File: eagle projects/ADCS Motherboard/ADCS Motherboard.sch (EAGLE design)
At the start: 143 parts, among them J1 HDR_10_EZFET_DEBUGGER, J11 CNC_3221-10-0300-00, J3 CNC_3221-10-0300-00, J5 CNC_3221-10-0300-00, J7 TE-1734829-3, J8 CNC_3221-10-0300-00, J9 CNC_3221-14-0300-00, Q1 PMV16XN, Q2 IRLML6246TRPBF, Q3 IRLML2246TRPBF, U1 MSP430F5529IPN, U2 LMV321, U3 ADS7841E_2K5, U4 LMV321, U5 LMV321, U7 HMC1053, Y1 32.768kHz, Y2 CSTCR4M00G15L99, Y3 32.768kHz

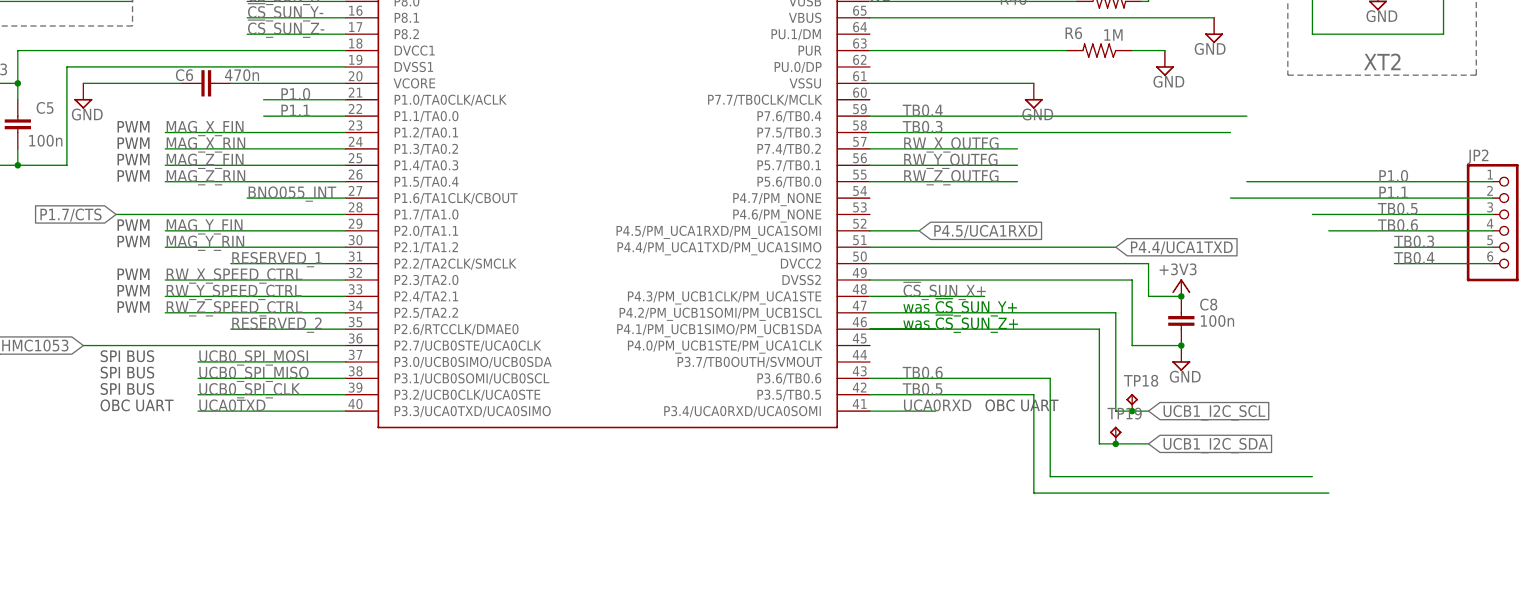
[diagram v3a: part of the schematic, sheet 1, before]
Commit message: Updated motherboad layout
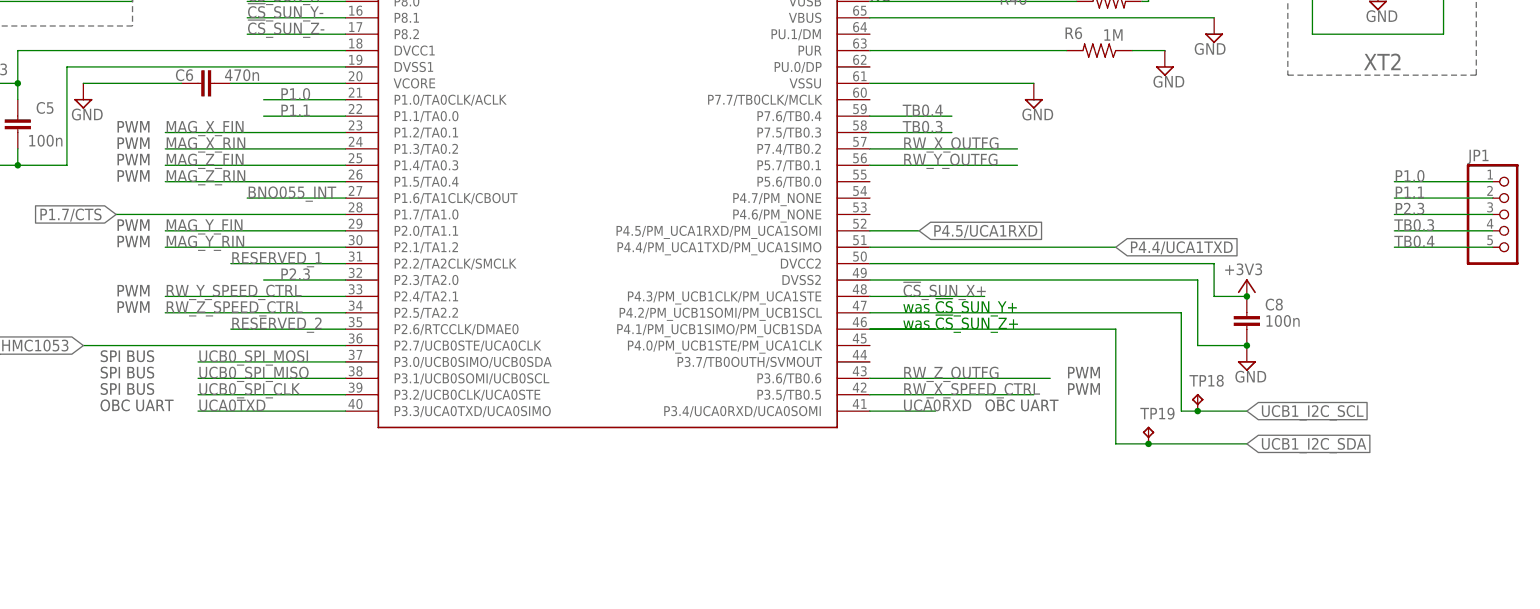
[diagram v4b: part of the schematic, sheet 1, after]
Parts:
- removed J10: (no value), my_library:PINHD-1X3
- removed JP2: (no value), my_library:PINHD-1X6
- removed R34, R35: 0R, rcl:R-US_R0805
- added JP1: (no value), my_library:PINHD-1X5
- R33: value 0R -> 5.1M; device rcl:R-US_R0805 -> rcl:R-US_R0402
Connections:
- removed net N$1: J10.1, R33.2
- removed net N$2: J10.2, R34.2
- removed net N$3: J10.3, R35.2
- removed net TB0.5: JP2.3, U1.P3.5/TB0.5
- removed net TB0.6: JP2.4, U1.P3.6/TB0.6
- new net P2.3: JP1.3, U1.P2.3/TA2.0
- net GND: now also R33.1
- net N$29: now also R33.2
- net P1.0: now also JP1.1; no longer JP2.1
- net P1.1: now also JP1.2; no longer JP2.2
- net RW_X_SPEED_CTRL: now also U1.P3.5/TB0.5; no longer U1.P2.3/TA2.0
- net RW_Z_OUTFG: now also U1.P3.6/TB0.6; no longer U1.P5.6/TB0.0
- net TB0.3: now also JP1.4; no longer JP2.5
- net TB0.4: now also JP1.5; no longer JP2.6
- net UCB0_SPI_CLK: no longer R33.1
- net UCB0_SPI_MISO: no longer R34.1
- net UCB0_SPI_MOSI: no longer R35.1
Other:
- moved on the sheet: C11, C8, C9, TP18, TP19

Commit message: Last commit before major layout changes on Actuator board Rev B
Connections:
- net !CS!_CURRENT_SENSE_1 renamed !CS!_CURR_SENSE_RW
- net !CS!_CURRENT_SENSE_2 renamed !CS!_CURR_SENSE_MTQR
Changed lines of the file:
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@@
 </segment>
 </net>
-<net name="!CS!_CURRENT_SENSE_1" class="0">
+<net name="!CS!_CURR_SENSE_RW" class="0">
 <segment>
 <pinref part="U1" gate="G$1" pin="P5.0/A8/VREF+/VEREF+"/>
@@
 </segment>
 </net>
-<net name="!CS!_CURRENT_SENSE_2" class="0">
+<net name="!CS!_CURR_SENSE_MTQR" class="0">
 <segment>
 <pinref part="U1" gate="G$1" pin="P5.1/A9/VREF-/VEREF-"/>
@@
 </segment>
 </net>
-<net name="!CS!_CURRENT_SENSE_1" class="0">
+<net name="!CS!_CURR_SENSE_RW" class="0">
 <segment>
 <pinref part="J8" gate="G$1" pin="3"/>
@@
 </segment>
 </net>
-<net name="!CS!_CURRENT_SENSE_2" class="0">
+<net name="!CS!_CURR_SENSE_MTQR" class="0">
 <segment>
 <pinref part="J8" gate="G$1" pin="5"/>
